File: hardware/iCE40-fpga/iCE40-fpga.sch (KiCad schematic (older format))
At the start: 49 parts, among them J1 USB_B_Micro, J2 JST_PH, J3 Feather, Q1 DMP2045U, U1 MCP73831-2-OT, U2 W25Q32JVZP, U3 AP2112K-3.3, U4 ICE40UP5K-SG48ITR, U5 NCV8114ASN120T1G, X1 DSC6101CI1A

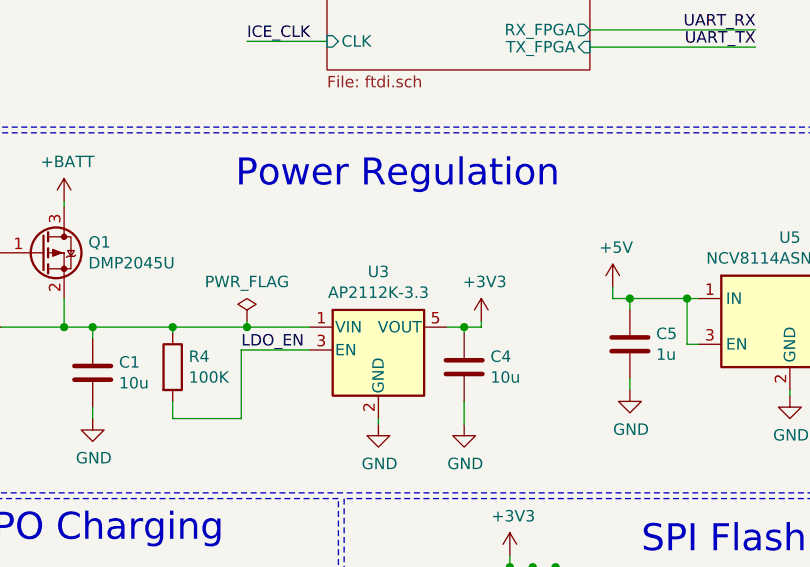
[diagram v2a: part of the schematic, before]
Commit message: fixed LED footprint + power supply change to support battery
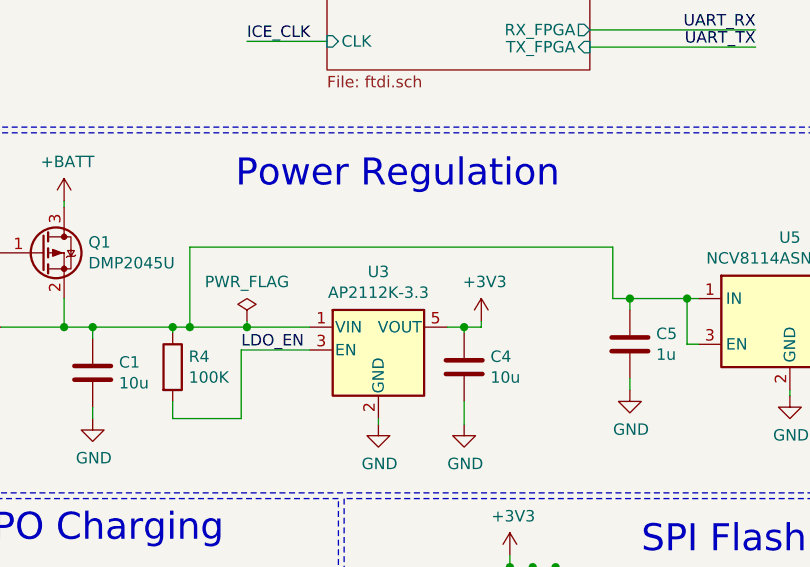
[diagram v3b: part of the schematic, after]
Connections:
- net +5V: no longer C5.1, U5.1 (IN), U5.3 (EN)
- net at C1.1, D2.1 (K), Q1.2 (S)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: now also C5.1, U5.1 (IN), U5.3 (EN)
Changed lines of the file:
@@
 Wire Wire Line
 	3750 3300 3675 3300
-Wire Wire Line
-	3675 3300 3675 3250
 Connection ~ 3750 3300
-$Comp
-L power:+5V #PWR026
-U 1 1 5D32F56D
-P 3675 3250
-F 0 "#PWR026" H 3675 3100 50  0001 C CNN
-F 1 "+5V" H 3690 3423 50  0000 C CNN
-F 2 "" H 3675 3250 50  0001 C CNN
-F 3 "" H 3675 3250 50  0001 C CNN
-	1    3675 3250
-	1    0    0    -1
-$EndComp
 Wire Wire Line
 	5000 3300 5000 3250
@@
 	9575 4500 9250 4500
 Wire Wire Line
-	1750 3425 2075 3425
+	1750 3425 1825 3425
 Connection ~ 1750 3425
 Wire Notes Line
@@
 Text Label 9300 4300 0    50   ~ 0
 IO_19
+Wire Wire Line
+	1825 3425 1825 3075
+Connection ~ 1825 3425
+Wire Wire Line
+	1825 3425 2075 3425
+Wire Wire Line
+	3675 3075 3675 3300
+Wire Wire Line
+	1825 3075 3675 3075
 $EndSCHEMATC

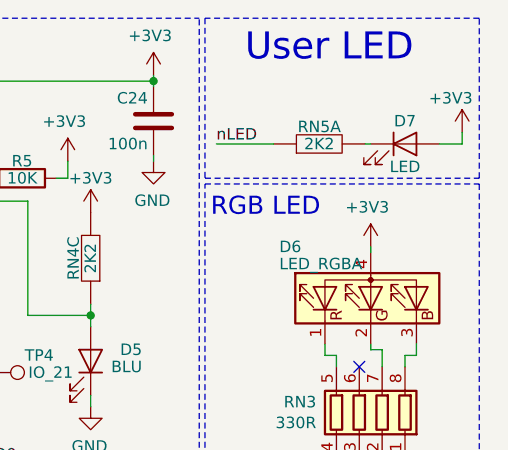
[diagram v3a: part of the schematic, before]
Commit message: generating BOM and costing things
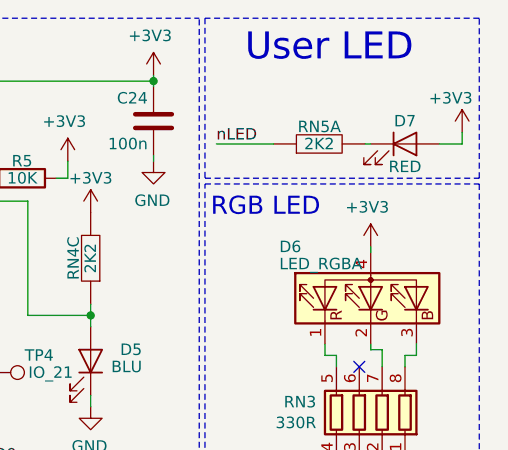
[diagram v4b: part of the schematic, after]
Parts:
- D7: value LED -> RED
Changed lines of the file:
@@
 P 10875 1050
 F 0 "D7" H 10875 1150 50  0000 C CNN
-F 1 "LED" H 10875 950 50  0000 C CNN
+F 1 "RED" H 10875 950 50  0000 C CNN
 F 2 "LED_SMD:LED_0603_1608Metric" H 10875 1050 50  0001 C CNN
 F 3 "~" H 10875 1050 50  0001 C CNN

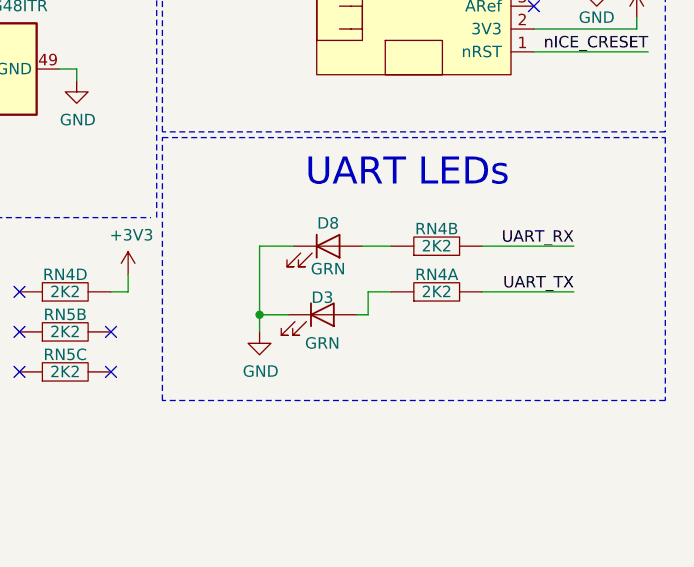
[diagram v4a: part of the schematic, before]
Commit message: changed TX RX led direction
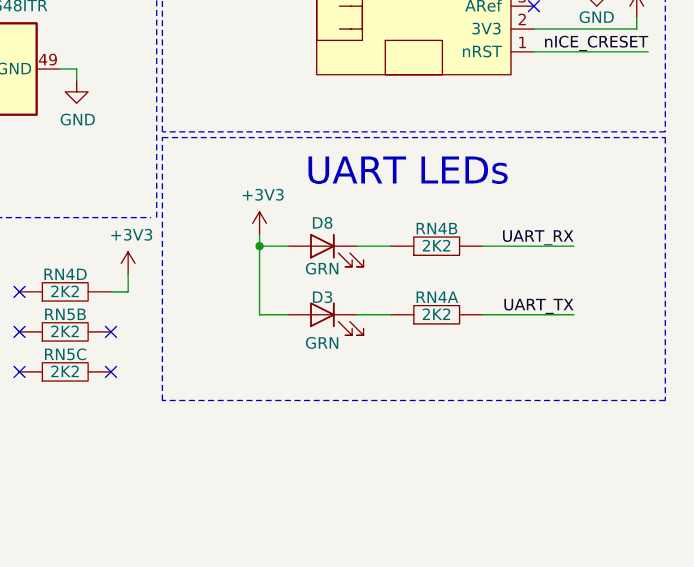
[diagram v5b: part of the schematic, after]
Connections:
- net +3V3: now also D3.2 (A), D8.2 (A)
- net GND: no longer D3.1 (K), D8.1 (K)
- net at RN4.3: now also D8.1 (K); no longer D8.2 (A)
- net at RN4.4: now also D3.1 (K); no longer D3.2 (A)
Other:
- moved on the sheet: D3, RN4A
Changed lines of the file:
@@
 L Device:LED D8
 U 1 1 5D13C806
-P 9725 5850
-F 0 "D8" H 9725 5950 50  0000 C CNN
-F 1 "GRN" H 9725 5750 50  0000 C CNN
-F 2 "LED_SMD:LED_0603_1608Metric" H 9725 5850 50  0001 C CNN
-F 3 "~" H 9725 5850 50  0001 C CNN
-	1    9725 5850
-	1    0    0    -1
-$EndComp
-Wire Wire Line
-	9575 5850 9425 5850
-Wire Wire Line
-	10800 6050 10400 6050
-$Comp
-L power:GND #PWR0107
-U 1 1 5D23BB88
-P 9425 6225
-F 0 "#PWR0107" H 9425 5975 50  0001 C CNN
-F 1 "GND" H 9430 6052 50  0000 C CNN
-F 2 "" H 9425 6225 50  0001 C CNN
-F 3 "" H 9425 6225 50  0001 C CNN
-	1    9425 6225
-	1    0    0    -1
-$EndComp
+P 9700 5850
+F 0 "D8" H 9700 5950 50  0000 C CNN
+F 1 "GRN" H 9700 5750 50  0000 C CNN
+F 2 "LED_SMD:LED_0603_1608Metric" H 9700 5850 50  0001 C CNN
+F 3 "~" H 9700 5850 50  0001 C CNN
+	1    9700 5850
+	-1   0    0    -1
+$EndComp
+Wire Wire Line
+	9550 5850 9425 5850
+Wire Wire Line
+	10800 6150 10400 6150
 Wire Notes Line
 	9000 5375 11200 5375
@@
 UART LEDs
 Wire Wire Line
-	9425 6150 9425 6225
-Connection ~ 9425 6150
-Wire Wire Line
 	9425 5850 9425 6150
 Wire Wire Line
 	9550 6150 9425 6150
-Wire Wire Line
-	9850 6150 9900 6150
 $Comp
 L Device:LED D3
@@
 F 3 "~" H 9700 6150 50  0001 C CNN
 	1    9700 6150
-	1    0    0    -1
-$EndComp
-Wire Wire Line
-	9900 6150 9900 6050
-Wire Wire Line
-	9900 6050 10000 6050
-Wire Wire Line
-	9875 5850 10000 5850
+	-1   0    0    -1
+$EndComp
+Wire Wire Line
+	9850 5850 10000 5850
 NoConn ~ 6900 1900
 NoConn ~ 8525 2250
@@
 L josh-passive:RN RN4
 U 1 1 5D43AB0E
-P 10200 6050
-F 0 "RN4" H 10200 6125 50  0000 C CNN
-F 1 "2K2" H 10200 6050 50  0000 C CNN
-F 2 "Resistor_SMD:R_Array_Convex_4x0402" V 10200 6050 50  0001 C CNN
-F 3 "~" V 10200 6050 50  0001 C CNN
-	1    10200 6050
+P 10200 6150
+F 0 "RN4" H 10200 6225 50  0000 C CNN
+F 1 "2K2" H 10200 6150 50  0000 C CNN
+F 2 "Resistor_SMD:R_Array_Convex_4x0402" V 10200 6150 50  0001 C CNN
+F 3 "~" V 10200 6150 50  0001 C CNN
+	1    10200 6150
 	1    0    0    -1
 $EndComp
@@
 Text Label 10800 5850 2    50   ~ 0
 UART_RX
-Text Label 10800 6050 2    50   ~ 0
+Text Label 10800 6150 2    50   ~ 0
 UART_TX
 Text Label 10775 2900 1    50   ~ 0
@@
 Wire Wire Line
 	1825 3075 3675 3075
+$Comp
+L power:+3V3 #PWR?
+U 1 1 5D415902
+P 9425 5800
+F 0 "#PWR?" H 9425 5650 50  0001 C CNN
+F 1 "+3V3" H 9440 5973 50  0000 C CNN
+F 2 "" H 9425 5800 50  0001 C CNN
+F 3 "" H 9425 5800 50  0001 C CNN
+	1    9425 5800
+	1    0    0    -1
+$EndComp
+Wire Wire Line
+	9425 5800 9425 5850
+Connection ~ 9425 5850
+Wire Wire Line
+	9850 6150 10000 6150
 $EndSCHEMATC
